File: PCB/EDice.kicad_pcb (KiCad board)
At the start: 2 copper layers, 65 x 30 mm, 24 parts, among them J2 Conn_01x04, J3 Conn_01x04, SW1 SW_Push, U1 PFS154-S16

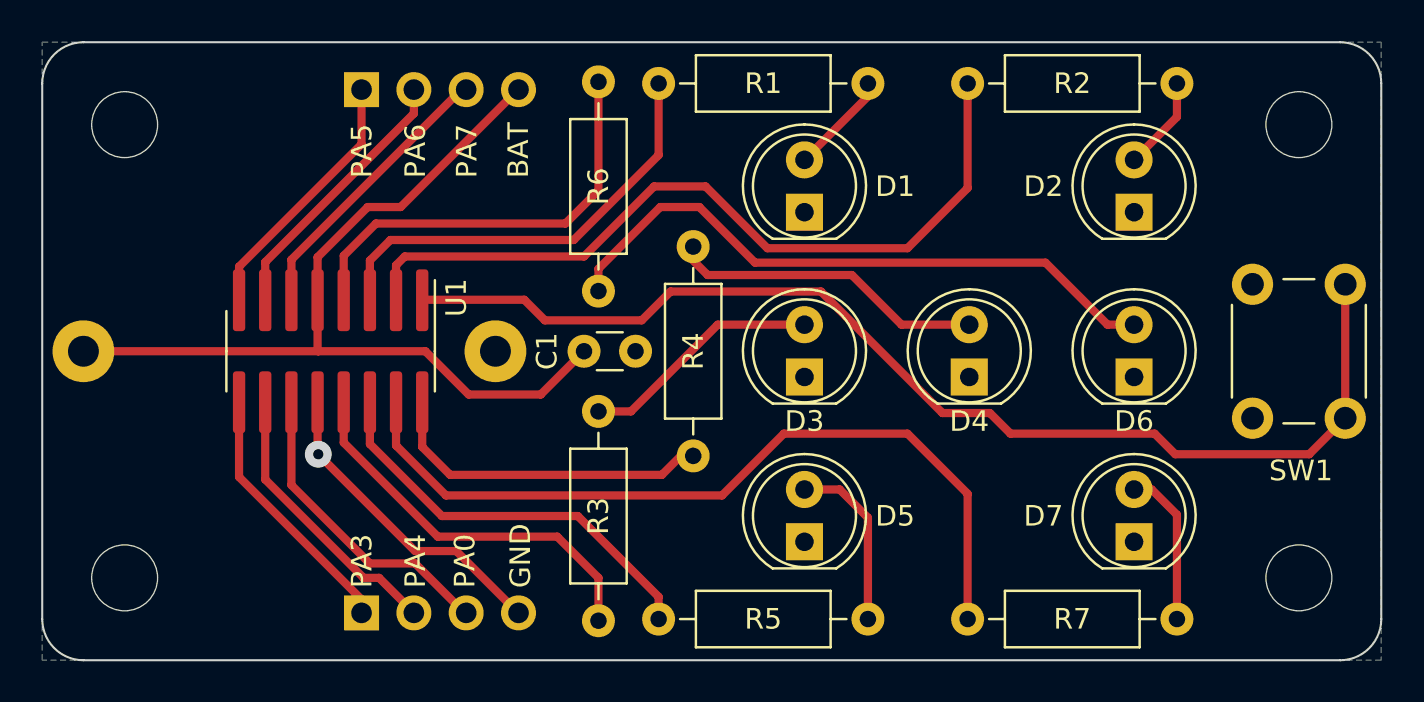
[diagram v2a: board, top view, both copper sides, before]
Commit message: swapped button to SMD and moved parts around
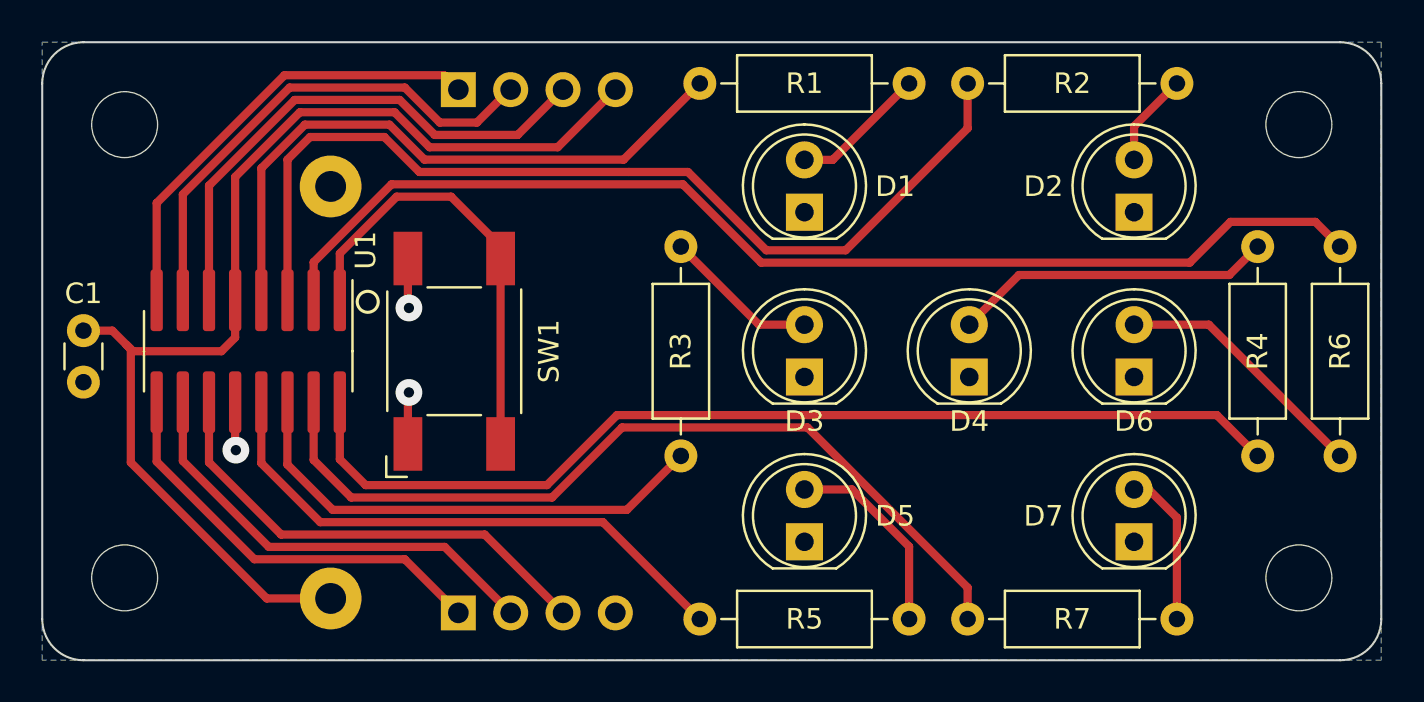
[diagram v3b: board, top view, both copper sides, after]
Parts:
- R1, R2, R3, R4, R5, R6, R7: value 560 -> 1k
- SW1: footprint Button_Switch_THT:SW_PUSH_6mm_H8mm -> EDice:K2-1102SP-J4SC-04
- moved SW1 38.9 mm to (113.0, 95.0)
- moved R6 36.9 mm to (156.0, 89.9)
- moved R4 27.4 mm to (152.0, 100.1)
- moved C1 24.3 mm to (95.0, 94.0), turned to -90 degrees
- moved R3 8.94 mm to (124.0, 100.1)
- moved J2 4.70 mm to (113.2, 82.3)
- moved J3 4.70 mm to (113.2, 107.7)
- moved U1 4.00 mm to (103.0, 95.0)
- moved R1 2.00 mm to (124.9, 82.0)
- moved R5 2.00 mm to (124.9, 108.0)
- moved BT1 0.14 mm to (107.0, 94.9), turned to -90 degrees
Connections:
- U1 pad 13: /LED3 -> /LED5
- U1 pad 14: /LED5 -> /LED3
- U1 pad 2: /LED2 -> /LED6
- U1 pad 3: /LED1 -> /LED2
- U1 pad 4: /LED6 -> /LED1
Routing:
- net /LED6: track 21.2 -> 56.1 mm
- net /BTN: track 56.3 -> 21.9 mm
- net /LED4: track 15.7 -> 50.1 mm
- net Net-(D6-A): track 30.7 -> 12.6 mm
- net /PA7: track 14.0 -> 26.1 mm
- net +BATT: track 43.8 -> 55.7 mm
- net /PA6: track 13.2 -> 24.6 mm
- net /PA5: track 12.7 -> 22.2 mm
- net /LED1: track 21.5 -> 30.8 mm
- net /LED2: track 38.6 -> 47.2 mm
- net /PA4: track 13.6 -> 21.8 mm
- net GND: track 15.5 -> 7.28 mm, vias 1 -> 3
- net /PA0: track 15.1 -> 23.1 mm
- net /PA3: track 12.7 -> 20.6 mm
- net /LED5: track 20.2 -> 27.4 mm
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
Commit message: aligned jumper pins to 1.27mm grid
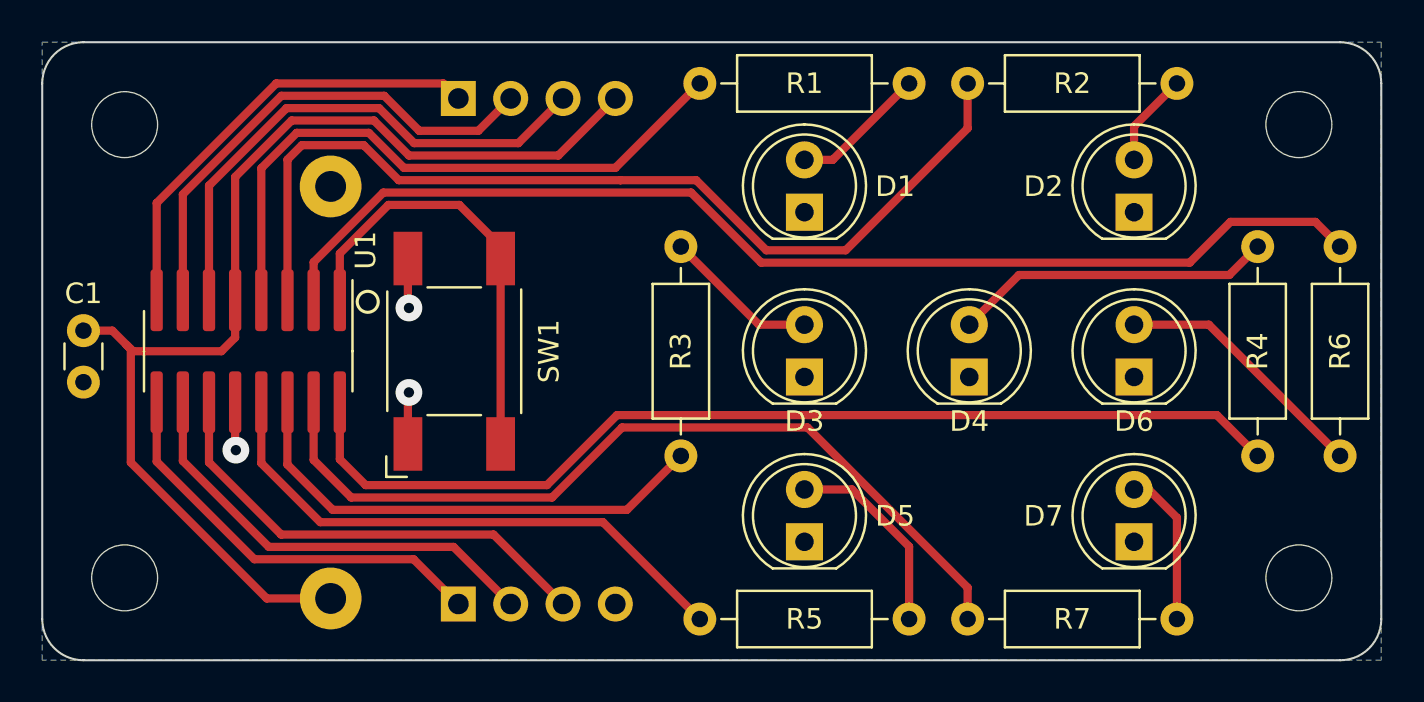
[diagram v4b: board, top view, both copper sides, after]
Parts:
- moved J2 0.43 mm to (113.2, 82.7)
- moved J3 0.43 mm to (113.2, 107.3)
